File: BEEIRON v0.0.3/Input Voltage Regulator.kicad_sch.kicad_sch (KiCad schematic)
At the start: 15 parts, among them J1 Conn_01x02_Male, U3 LP2985-3.3, U4 NCP1117-5.0_SOT223

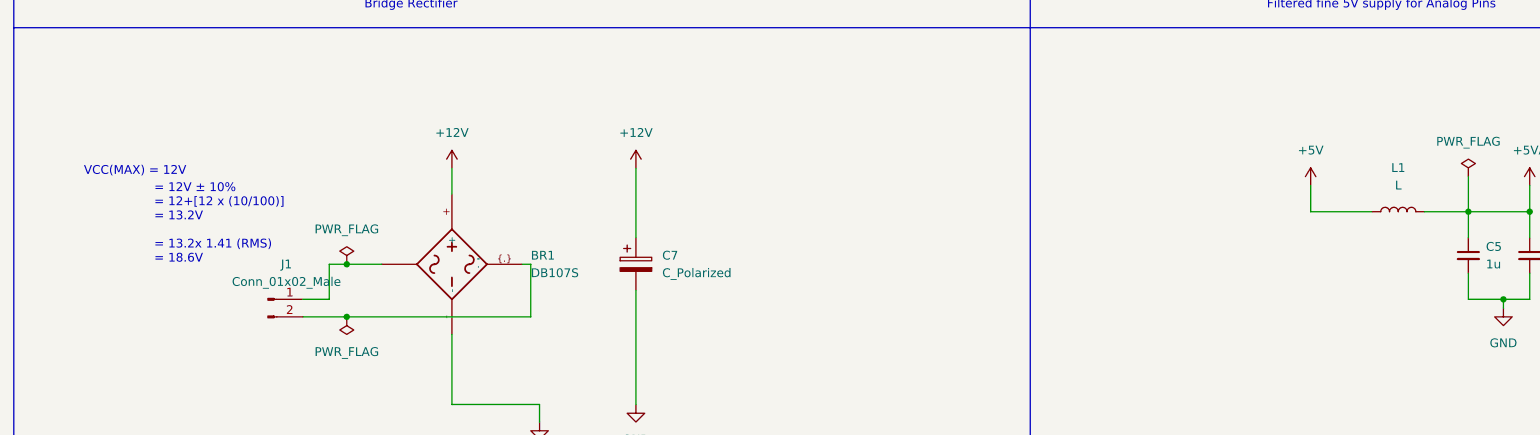
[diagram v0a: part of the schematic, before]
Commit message: minor edit in the schematics
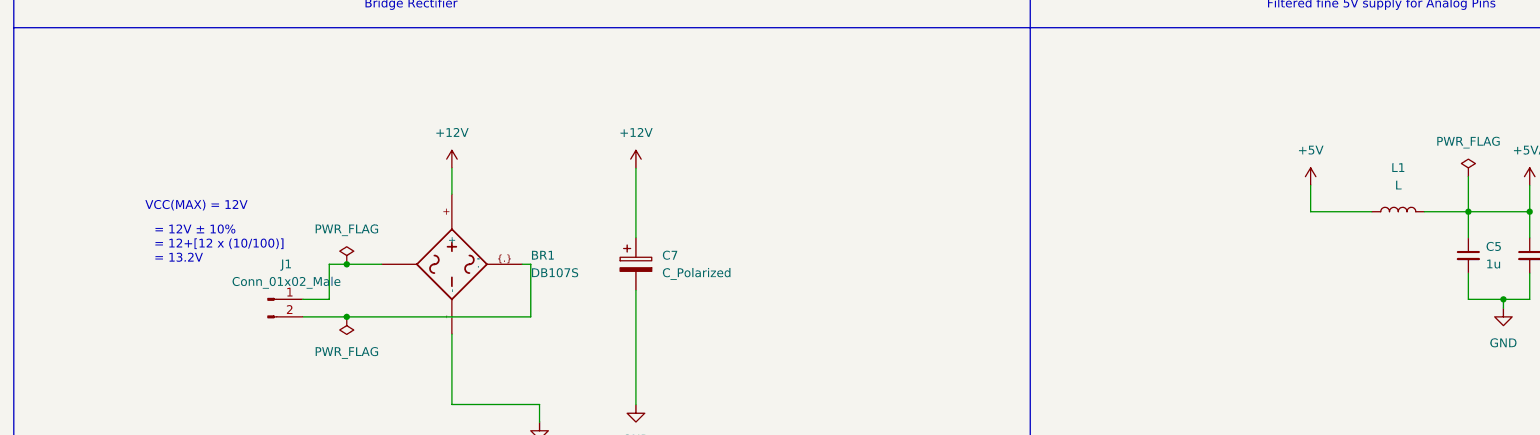
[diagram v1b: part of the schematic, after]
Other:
- note added: "= 12V ± 10% = 12+[12 x (10/100)] = 13.2V"
- note removed: "= 12V ± 10% = 12+[12 x (10/100)] = 13.2V = 13.2x 1.41 (RMS) = 18.6V"
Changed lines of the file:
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@@
     (stroke (width 0) (type default) (color 0 0 0 0))
   )
-  (text "VCC(MAX) = 12V" (at 22.86 121.92 0)
-    (effects (font (size 1.27 1.27)) (justify left bottom))
-  )
-  (text "= 12V ± 10%\n= 12+[12 x (10/100)]\n= 13.2V\n\n= 13.2x 1.41 (RMS)\n= 18.6V"
-    (at 33.045 134.6382 0)
+  (text "VCC(MAX) = 12V" (at 31.75 127 0)
+    (effects (font (size 1.27 1.27)) (justify left bottom))
+  )
+  (text "= 12V ± 10%\n= 12+[12 x (10/100)]\n= 13.2V" (at 33.045 134.6382 0)
     (effects (font (size 1.27 1.27)) (justify left bottom))
   )
@@
     )
     (property "Datasheet" "~" (id 3) (at 60.96 142.24 0)
-      (effects (font (size 1.27 1.27)) hide)
-    )
-    (pin "1")
-  )
-  (symbol (lib_id "power:PWR_FLAG") (at 78.74 49.53 0) (unit 1)
-    (in_bom yes) (on_board yes) (fields_autoplaced)
-    (property "Reference" "#FLG01" (id 0) (at 78.74 47.625 0)
-      (effects (font (size 1.27 1.27)) hide)
-    )
-    (property "Value" "PWR_FLAG" (id 1) (at 78.74 44.45 0))
-    (property "Footprint" "" (id 2) (at 78.74 49.53 0)
-      (effects (font (size 1.27 1.27)) hide)
-    )
-    (property "Datasheet" "~" (id 3) (at 78.74 49.53 0)
-      (effects (font (size 1.27 1.27)) hide)
-    )
-    (pin "1")
-  )
-  (symbol (lib_id "power:PWR_FLAG") (at 223.52 121.92 0) (unit 1)
-    (in_bom yes) (on_board yes) (fields_autoplaced)
-    (property "Reference" "#FLG02" (id 0) (at 223.52 120.015 0)
-      (effects (font (size 1.27 1.27)) hide)
-    )
-    (property "Value" "PWR_FLAG" (id 1) (at 223.52 116.84 0))
-    (property "Footprint" "" (id 2) (at 223.52 121.92 0)
-      (effects (font (size 1.27 1.27)) hide)
-    )
-    (property "Datasheet" "~" (id 3) (at 223.52 121.92 0)
       (effects (font (size 1.27 1.27)) hide)
     )
@@
     (pin "2")
   )
+  (symbol (lib_id "power:PWR_FLAG") (at 78.74 49.53 0) (unit 1)
+    (in_bom yes) (on_board yes) (fields_autoplaced)
+    (property "Reference" "#FLG01" (id 0) (at 78.74 47.625 0)
+      (effects (font (size 1.27 1.27)) hide)
+    )
+    (property "Value" "PWR_FLAG" (id 1) (at 78.74 44.45 0))
+    (property "Footprint" "" (id 2) (at 78.74 49.53 0)
+      (effects (font (size 1.27 1.27)) hide)
+    )
+    (property "Datasheet" "~" (id 3) (at 78.74 49.53 0)
+      (effects (font (size 1.27 1.27)) hide)
+    )
+    (pin "1")
+  )
+  (symbol (lib_id "power:PWR_FLAG") (at 223.52 121.92 0) (unit 1)
+    (in_bom yes) (on_board yes) (fields_autoplaced)
+    (property "Reference" "#FLG02" (id 0) (at 223.52 120.015 0)
+      (effects (font (size 1.27 1.27)) hide)
+    )
+    (property "Value" "PWR_FLAG" (id 1) (at 223.52 116.84 0))
+    (property "Footprint" "" (id 2) (at 223.52 121.92 0)
+      (effects (font (size 1.27 1.27)) hide)
+    )
+    (property "Datasheet" "~" (id 3) (at 223.52 121.92 0)
+      (effects (font (size 1.27 1.27)) hide)
+    )
+    (pin "1")
+  )
   (symbol (lib_id "power:GND") (at 78.74 69.85 0) (unit 1)
